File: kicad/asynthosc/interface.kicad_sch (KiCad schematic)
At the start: 21 parts, among them SW10 SW_MEC_5G_LED, SW8 RotaryEncoder, SW9 SW_MEC_5G_LED

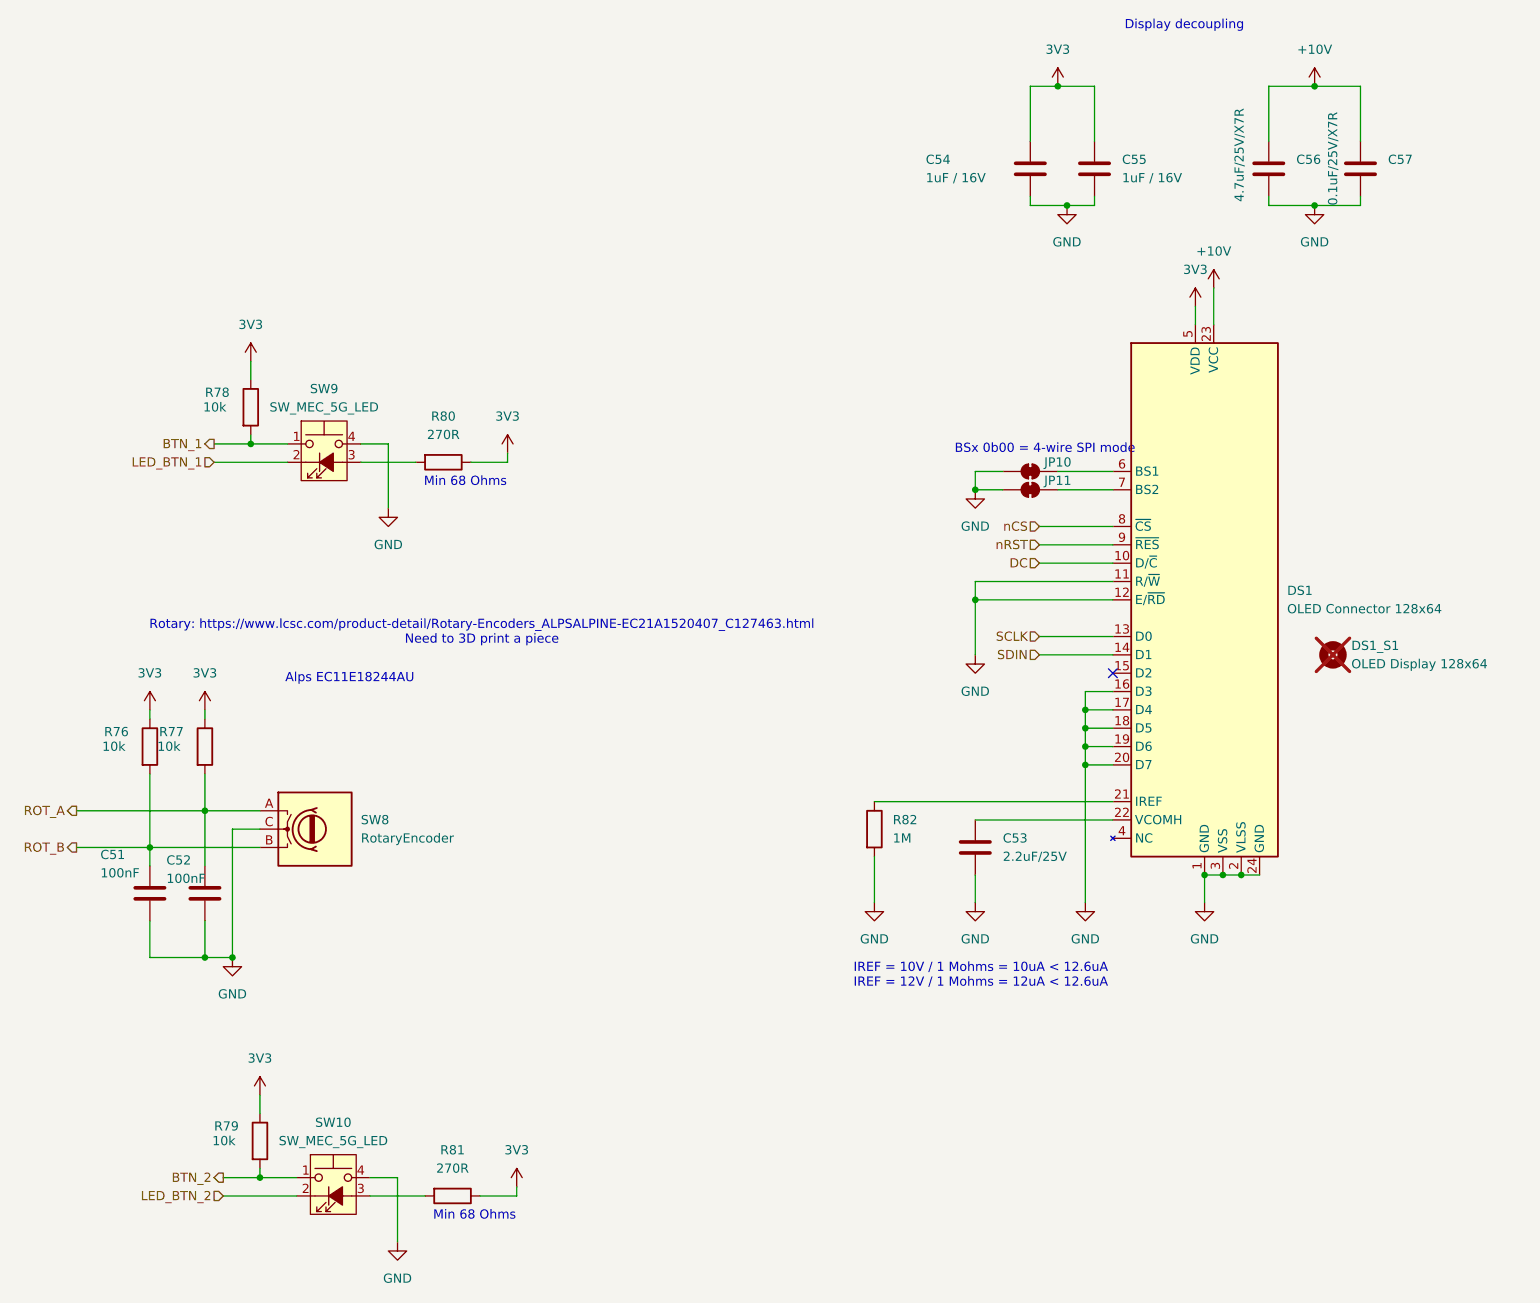
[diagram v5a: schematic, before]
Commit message: pcb: place and change some components for easier routing
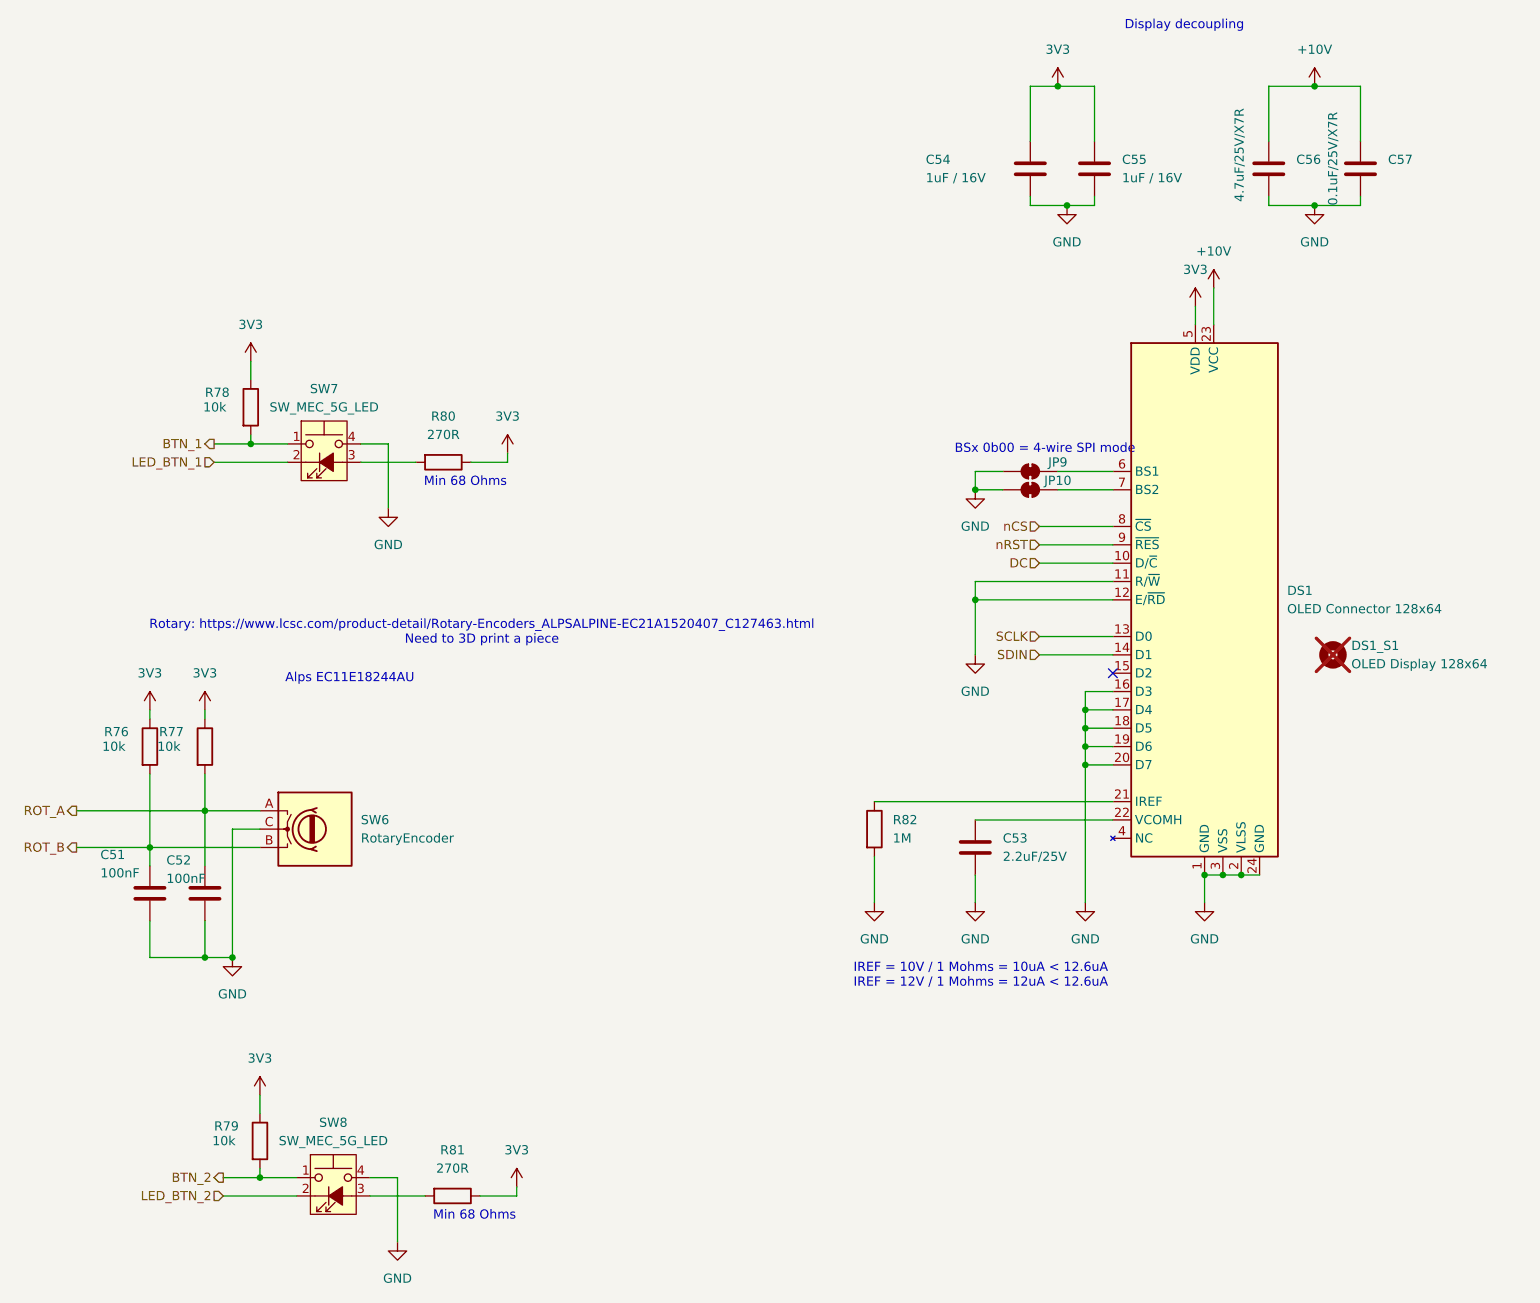
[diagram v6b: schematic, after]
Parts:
- renumbered JP11 to JP10, JP10 to JP9, SW8 to SW6, SW9 to SW7, SW10 to SW8
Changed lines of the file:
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@@
 		(dnp no)
 		(fields_autoplaced yes)
-		(property "Reference" "#PWR0141"
+		(property "Reference" "#PWR0144"
 			(at 182.88 142.24 0)
 			(effects
@@
 			(project ""
 				(path "/d73e377a-a016-415f-8824-91cc6e4907b9/b863f609-74bc-4dca-9f89-b76b25b90e2d"
-					(reference "#PWR0141")
+					(reference "#PWR0144")
 					(unit 1)
 				)
@@
 		(dnp no)
 		(fields_autoplaced yes)
-		(property "Reference" "#PWR0138"
+		(property "Reference" "#PWR0141"
 			(at 163.83 45.72 0)
 			(effects
@@
 			(project "asynthosc"
 				(path "/d73e377a-a016-415f-8824-91cc6e4907b9/b863f609-74bc-4dca-9f89-b76b25b90e2d"
-					(reference "#PWR0138")
+					(reference "#PWR0141")
 					(unit 1)
 				)
@@
 		(dnp no)
 		(fields_autoplaced yes)
-		(property "Reference" "#PWR0126"
+		(property "Reference" "#PWR0129"
 			(at 48.26 149.86 0)
 			(effects
@@
 			(project "asynthosc"
 				(path "/d73e377a-a016-415f-8824-91cc6e4907b9/b863f609-74bc-4dca-9f89-b76b25b90e2d"
-					(reference "#PWR0126")
+					(reference "#PWR0129")
 					(unit 1)
 				)
@@
 		(dnp no)
 		(fields_autoplaced yes)
-		(property "Reference" "#PWR0135"
+		(property "Reference" "#PWR0138"
 			(at 151.13 107.95 0)
 			(effects
@@
 			(project "asynthosc"
 				(path "/d73e377a-a016-415f-8824-91cc6e4907b9/b863f609-74bc-4dca-9f89-b76b25b90e2d"
-					(reference "#PWR0135")
+					(reference "#PWR0138")
 					(unit 1)
 				)
@@
 		(dnp no)
 		(fields_autoplaced yes)
-		(property "Reference" "#PWR0128"
+		(property "Reference" "#PWR0131"
 			(at 52.07 166.37 0)
 			(effects
@@
 			(project "asynthosc"
 				(path "/d73e377a-a016-415f-8824-91cc6e4907b9/b863f609-74bc-4dca-9f89-b76b25b90e2d"
-					(reference "#PWR0128")
+					(reference "#PWR0131")
 					(unit 1)
 				)
@@
 		(dnp no)
 		(fields_autoplaced yes)
-		(property "Reference" "#PWR0127"
+		(property "Reference" "#PWR0130"
 			(at 50.8 64.77 0)
 			(effects
@@
 			(project "asynthosc"
 				(path "/d73e377a-a016-415f-8824-91cc6e4907b9/b863f609-74bc-4dca-9f89-b76b25b90e2d"
-					(reference "#PWR0127")
+					(reference "#PWR0130")
 					(unit 1)
 				)
@@
 		(dnp no)
 		(fields_autoplaced yes)
-		(property "Reference" "#PWR0132"
+		(property "Reference" "#PWR0135"
 			(at 87.63 179.07 0)
 			(effects
@@
 			(project "asynthosc"
 				(path "/d73e377a-a016-415f-8824-91cc6e4907b9/b863f609-74bc-4dca-9f89-b76b25b90e2d"
-					(reference "#PWR0132")
+					(reference "#PWR0135")
 					(unit 1)
 				)
@@
 		(dnp no)
 		(fields_autoplaced yes)
-		(property "Reference" "#PWR0144"
+		(property "Reference" "#PWR0147"
 			(at 198.12 45.72 0)
 			(effects
@@
 			(project "asynthosc"
 				(path "/d73e377a-a016-415f-8824-91cc6e4907b9/b863f609-74bc-4dca-9f89-b76b25b90e2d"
-					(reference "#PWR0144")
+					(reference "#PWR0147")
 					(unit 1)
 				)
@@
 		(dnp no)
 		(fields_autoplaced yes)
-		(property "Reference" "#PWR0139"
+		(property "Reference" "#PWR0142"
 			(at 166.37 142.24 0)
 			(effects
@@
 			(project "asynthosc"
 				(path "/d73e377a-a016-415f-8824-91cc6e4907b9/b863f609-74bc-4dca-9f89-b76b25b90e2d"
-					(reference "#PWR0139")
+					(reference "#PWR0142")
 					(unit 1)
 				)
@@
 		(dnp no)
 		(fields_autoplaced yes)
-		(property "Reference" "#PWR0134"
+		(property "Reference" "#PWR0137"
 			(at 151.13 85.09 0)
 			(effects
@@
 			(project "asynthosc"
 				(path "/d73e377a-a016-415f-8824-91cc6e4907b9/b863f609-74bc-4dca-9f89-b76b25b90e2d"
-					(reference "#PWR0134")
+					(reference "#PWR0137")
 					(unit 1)
 				)
@@
 		(dnp no)
 		(fields_autoplaced yes)
-		(property "Reference" "#PWR0125"
+		(property "Reference" "#PWR0128"
 			(at 44.45 113.03 0)
 			(effects
@@
 			(project "asynthosc"
 				(path "/d73e377a-a016-415f-8824-91cc6e4907b9/b863f609-74bc-4dca-9f89-b76b25b90e2d"
-					(reference "#PWR0125")
+					(reference "#PWR0128")
 					(unit 1)
 				)
@@
 		(dnp no)
 		(fields_autoplaced yes)
-		(property "Reference" "#PWR0131"
+		(property "Reference" "#PWR0134"
 			(at 86.36 77.47 0)
 			(effects
@@
 			(project "asynthosc"
 				(path "/d73e377a-a016-415f-8824-91cc6e4907b9/b863f609-74bc-4dca-9f89-b76b25b90e2d"
-					(reference "#PWR0131")
+					(reference "#PWR0134")
 					(unit 1)
 				)
@@
 		(dnp no)
 		(fields_autoplaced yes)
-		(property "Reference" "#PWR0142"
+		(property "Reference" "#PWR0145"
 			(at 184.15 54.61 0)
 			(effects
@@
 			(project "asynthosc"
 				(path "/d73e377a-a016-415f-8824-91cc6e4907b9/b863f609-74bc-4dca-9f89-b76b25b90e2d"
-					(reference "#PWR0142")
+					(reference "#PWR0145")
 					(unit 1)
 				)
@@
 		(dnp no)
 		(fields_autoplaced yes)
-		(property "Reference" "#PWR0133"
+		(property "Reference" "#PWR0136"
 			(at 137.16 142.24 0)
 			(effects
@@
 			(project "asynthosc"
 				(path "/d73e377a-a016-415f-8824-91cc6e4907b9/b863f609-74bc-4dca-9f89-b76b25b90e2d"
-					(reference "#PWR0133")
+					(reference "#PWR0136")
 					(unit 1)
 				)
@@
 		(dnp no)
 		(fields_autoplaced yes)
-		(property "Reference" "#PWR0140"
+		(property "Reference" "#PWR0143"
 			(at 181.61 57.15 0)
 			(effects
@@
 			(project "asynthosc"
 				(path "/d73e377a-a016-415f-8824-91cc6e4907b9/b863f609-74bc-4dca-9f89-b76b25b90e2d"
-					(reference "#PWR0140")
+					(reference "#PWR0143")
 					(unit 1)
 				)
@@
 		(dnp no)
 		(fields_autoplaced yes)
-		(property "Reference" "SW9"
+		(property "Reference" "SW7"
 			(at 60.96 64.77 0)
 			(effects
@@
 			(project ""
 				(path "/d73e377a-a016-415f-8824-91cc6e4907b9/b863f609-74bc-4dca-9f89-b76b25b90e2d"
-					(reference "SW9")
+					(reference "SW7")
 					(unit 1)
 				)
@@
 		(dnp no)
 		(fields_autoplaced yes)
-		(property "Reference" "#PWR0136"
+		(property "Reference" "#PWR0139"
 			(at 151.13 142.24 0)
 			(effects
@@
 			(project "asynthosc"
 				(path "/d73e377a-a016-415f-8824-91cc6e4907b9/b863f609-74bc-4dca-9f89-b76b25b90e2d"
-					(reference "#PWR0136")
+					(reference "#PWR0139")
 					(unit 1)
 				)
@@
 		(dnp no)
 		(fields_autoplaced yes)
-		(property "Reference" "#PWR0143"
+		(property "Reference" "#PWR0146"
 			(at 198.12 26.67 0)
 			(effects
@@
 			(project ""
 				(path "/d73e377a-a016-415f-8824-91cc6e4907b9/b863f609-74bc-4dca-9f89-b76b25b90e2d"
-					(reference "#PWR0143")
+					(reference "#PWR0146")
 					(unit 1)
 				)
@@
 		(dnp no)
 		(fields_autoplaced yes)
-		(property "Reference" "#PWR0137"
+		(property "Reference" "#PWR0140"
 			(at 162.56 26.67 0)
 			(effects
@@
 			(project "asynthosc"
 				(path "/d73e377a-a016-415f-8824-91cc6e4907b9/b863f609-74bc-4dca-9f89-b76b25b90e2d"
-					(reference "#PWR0137")
+					(reference "#PWR0140")
 					(unit 1)
 				)
@@
 		(dnp no)
 		(fields_autoplaced yes)
-		(property "Reference" "SW8"
+		(property "Reference" "SW6"
 			(at 66.04 124.4599 0)
 			(effects
@@
 			(project ""
 				(path "/d73e377a-a016-415f-8824-91cc6e4907b9/b863f609-74bc-4dca-9f89-b76b25b90e2d"
-					(reference "SW8")
+					(reference "SW6")
 					(unit 1)
 				)
@@
 		(dnp no)
 		(fields_autoplaced yes)
-		(property "Reference" "#PWR0124"
+		(property "Reference" "#PWR0127"
 			(at 36.83 113.03 0)
 			(effects
@@
 			(project "asynthosc"
 				(path "/d73e377a-a016-415f-8824-91cc6e4907b9/b863f609-74bc-4dca-9f89-b76b25b90e2d"
-					(reference "#PWR0124")
+					(reference "#PWR0127")
 					(unit 1)
 				)
@@
 		(dnp no)
 		(fields_autoplaced yes)
-		(property "Reference" "#PWR0129"
+		(property "Reference" "#PWR0132"
 			(at 69.85 87.63 0)
 			(effects
@@
 			(project "asynthosc"
 				(path "/d73e377a-a016-415f-8824-91cc6e4907b9/b863f609-74bc-4dca-9f89-b76b25b90e2d"
-					(reference "#PWR0129")
+					(reference "#PWR0132")
 					(unit 1)
 				)
@@
 		(on_board yes)
 		(dnp no)
-		(property "Reference" "JP10"
+		(property "Reference" "JP9"
 			(at 162.56 74.93 0)
 			(effects
@@
 			(project ""
 				(path "/d73e377a-a016-415f-8824-91cc6e4907b9/b863f609-74bc-4dca-9f89-b76b25b90e2d"
-					(reference "JP10")
+					(reference "JP9")
 					(unit 1)
 				)
@@
 		(dnp no)
 		(fields_autoplaced yes)
-		(property "Reference" "#PWR0130"
+		(property "Reference" "#PWR0133"
 			(at 71.12 189.23 0)
 			(effects
@@
 			(project "asynthosc"
 				(path "/d73e377a-a016-415f-8824-91cc6e4907b9/b863f609-74bc-4dca-9f89-b76b25b90e2d"
-					(reference "#PWR0130")
+					(reference "#PWR0133")
 					(unit 1)
 				)
@@
 		(on_board yes)
 		(dnp no)
-		(property "Reference" "JP11"
+		(property "Reference" "JP10"
 			(at 162.56 77.47 0)
 			(effects
@@
 			(project "asynthosc"
 				(path "/d73e377a-a016-415f-8824-91cc6e4907b9/b863f609-74bc-4dca-9f89-b76b25b90e2d"
-					(reference "JP11")
+					(reference "JP10")
 					(unit 1)
 				)
@@
 		(dnp no)
 		(fields_autoplaced yes)
-		(property "Reference" "SW10"
+		(property "Reference" "SW8"
 			(at 62.23 166.37 0)
 			(effects
@@
 			(project "asynthosc"
 				(path "/d73e377a-a016-415f-8824-91cc6e4907b9/b863f609-74bc-4dca-9f89-b76b25b90e2d"
-					(reference "SW10")
+					(reference "SW8")
 					(unit 1)
 				)

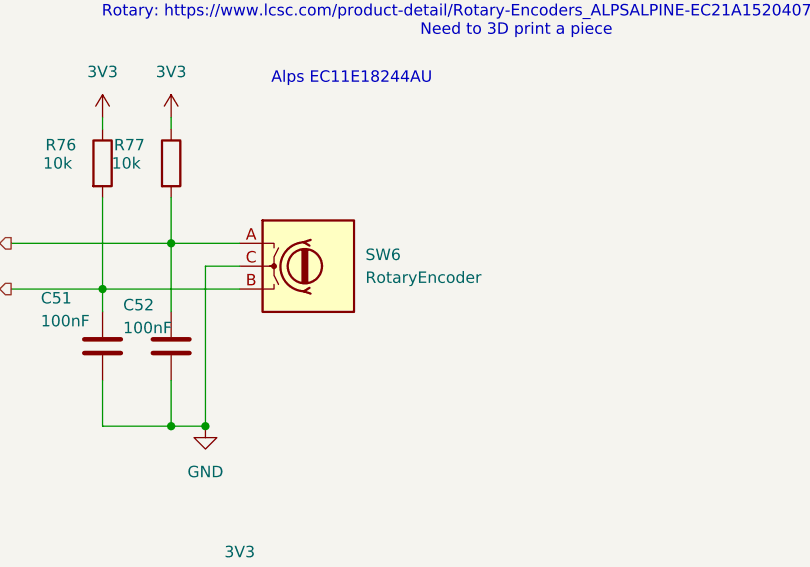
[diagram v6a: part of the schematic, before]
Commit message: sch: pcb: fix: footprint mismatches
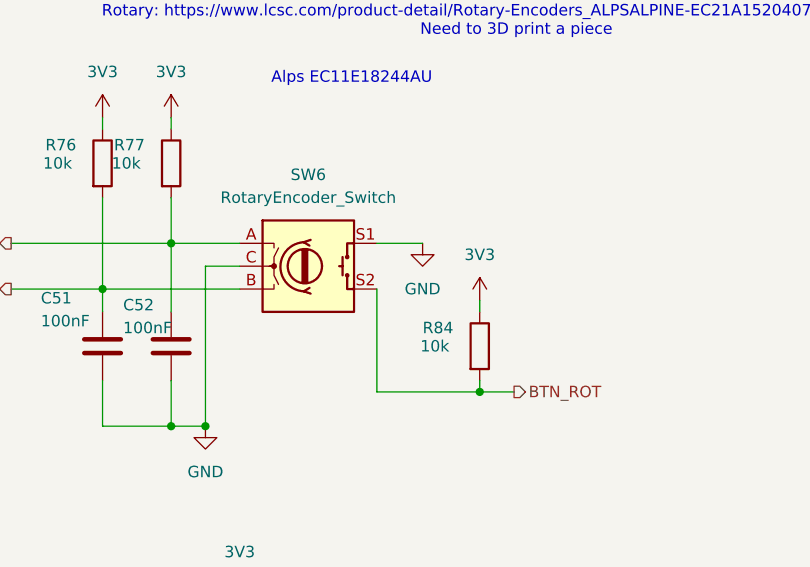
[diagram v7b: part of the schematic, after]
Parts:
- removed SW6: RotaryEncoder, Rotary_Encoder:RotaryEncoder_Alps_EC12E_Vertical_H20mm, symbol Device:RotaryEncoder
- added R84: 10k, Resistor_SMD:R_0402_1005Metric, symbol Device:R
- added SW6: RotaryEncoder_Switch, Rotary_Encoder:RotaryEncoder_Alps_EC11E-Switch_Vertical_H20mm, symbol Device:RotaryEncoder_Switch
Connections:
- net 3V3: now also R84.1
- net GND: now also SW6.C, SW6.S1
- net ROT_A: now also SW6.A
- net ROT_B: now also SW6.B
- new net BTN_ROT: R84.2, SW6.S2

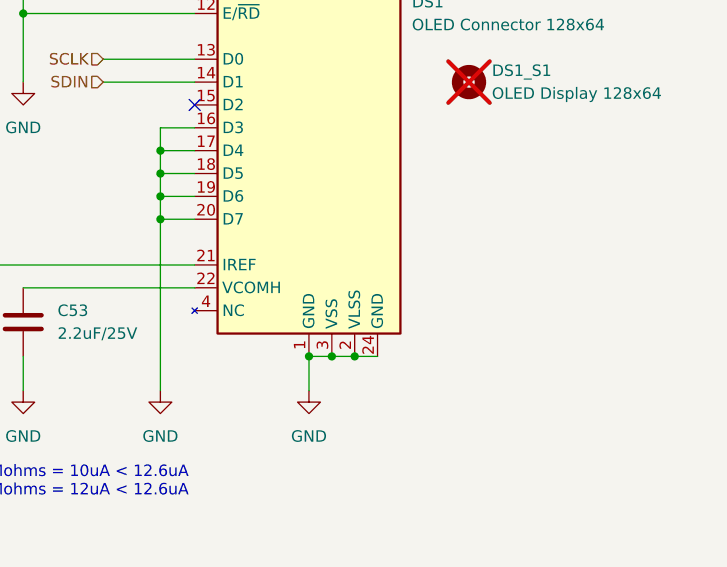
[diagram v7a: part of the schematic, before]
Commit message: pcb: sch: drown mp pad in gnd for display connector
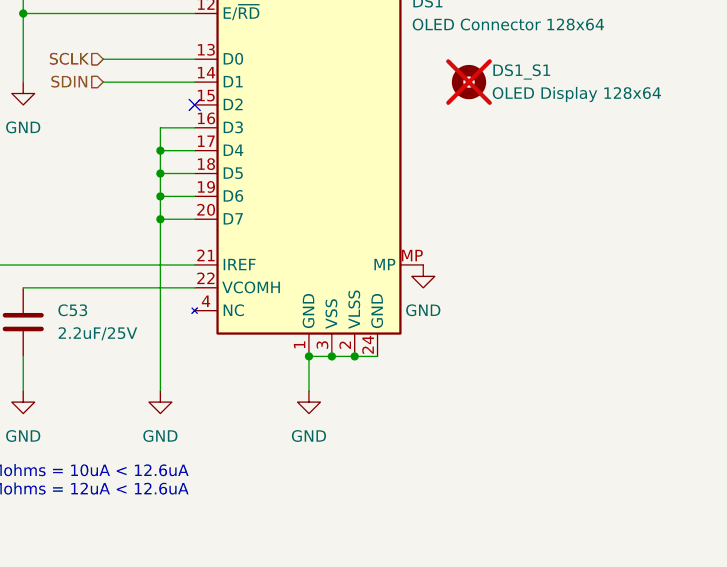
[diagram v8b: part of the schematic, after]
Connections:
- net GND: now also DS1.MP
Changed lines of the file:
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@@
 		(pin "15"
+		)
+		(pin "MP"
 		)
 		(instances
@@
 					(unit 1)
 				)
+			)
+		)
+	)
+	(symbol
+		(lib_id "power:GND")
+		(at 195.58 121.92 0)
+		(unit 1)
+		(exclude_from_sim no)
+		(in_bom yes)
+		(on_board yes)
+		(dnp no)
+		(fields_autoplaced yes)
+		(property "Reference" "#PWR0159"
+			(at 195.58 128.27 0)
+			(effects
+				(font
+					(size 1.27 1.27)
+				)
+				(hide yes)
+			)
+		)
+		(property "Value" "GND"
+			(at 195.58 127 0)
+			(effects
+				(font
+					(size 1.27 1.27)
+				)
+			)
+		)
+		(property "Footprint" ""
+			(at 195.58 121.92 0)
+			(effects
+				(font
+					(size 1.27 1.27)
+				)
+				(hide yes)
+			)
+		)
+		(property "Datasheet" ""
+			(at 195.58 121.92 0)
+			(effects
+				(font
+					(size 1.27 1.27)
+				)
+				(hide yes)
+			)
+		)
+		(property "Description" "Power symbol creates a global label with name \"GND\" , ground"
+			(at 195.58 121.92 0)
+			(effects
+				(font
+					(size 1.27 1.27)
+				)
+				(hide yes)
+			)
+		)
+		(pin "1"
+		)
+		(instances
+			(project "asynthosc"
+				(path "/d73e377a-a016-415f-8824-91cc6e4907b9/b863f609-74bc-4dca-9f89-b76b25b90e2d"
+					(reference "#PWR0159")
+					(unit 1)
+				)
